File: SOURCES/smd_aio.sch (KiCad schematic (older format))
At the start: 44 parts, among them P2 CONN_01X03, P3 CONN_02X05, P4 STDCONN, Q1 BSS123, Q2 BSS123, Q3 BSS123, Q4 BSS123, Q5 FZT751TA, SW1 SW_PUSH, U2 24AA256SN

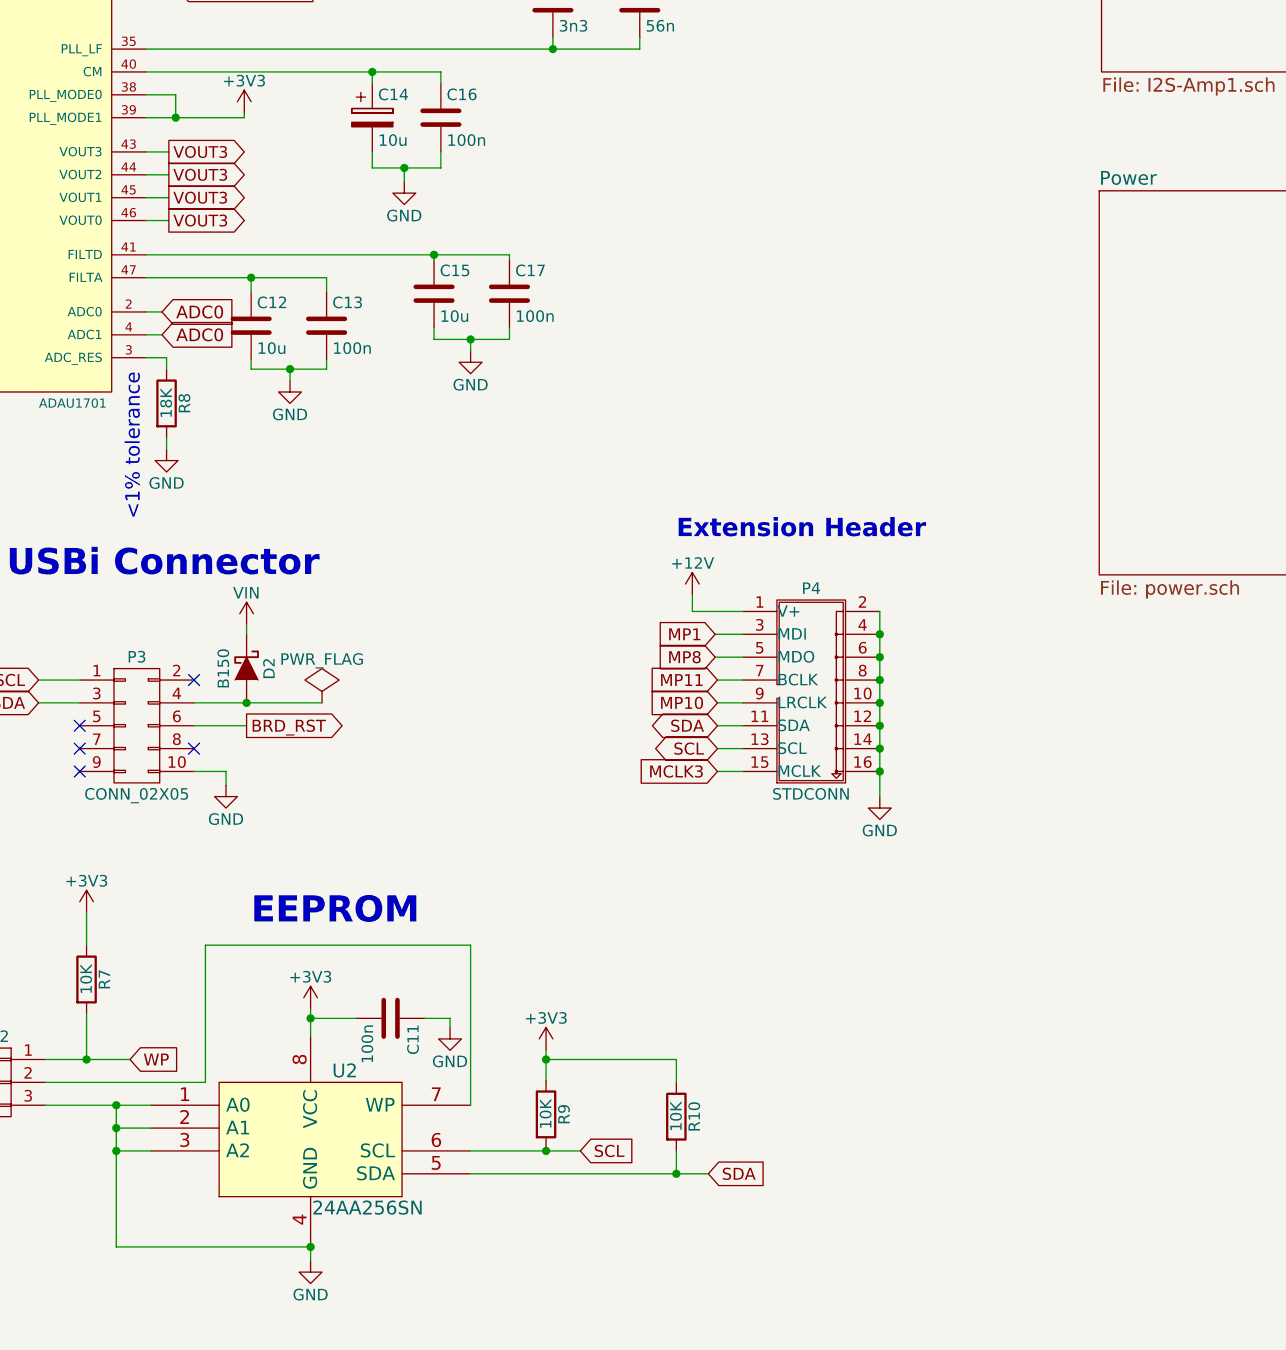
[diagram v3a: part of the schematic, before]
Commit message: added SPDIF lib & analog out
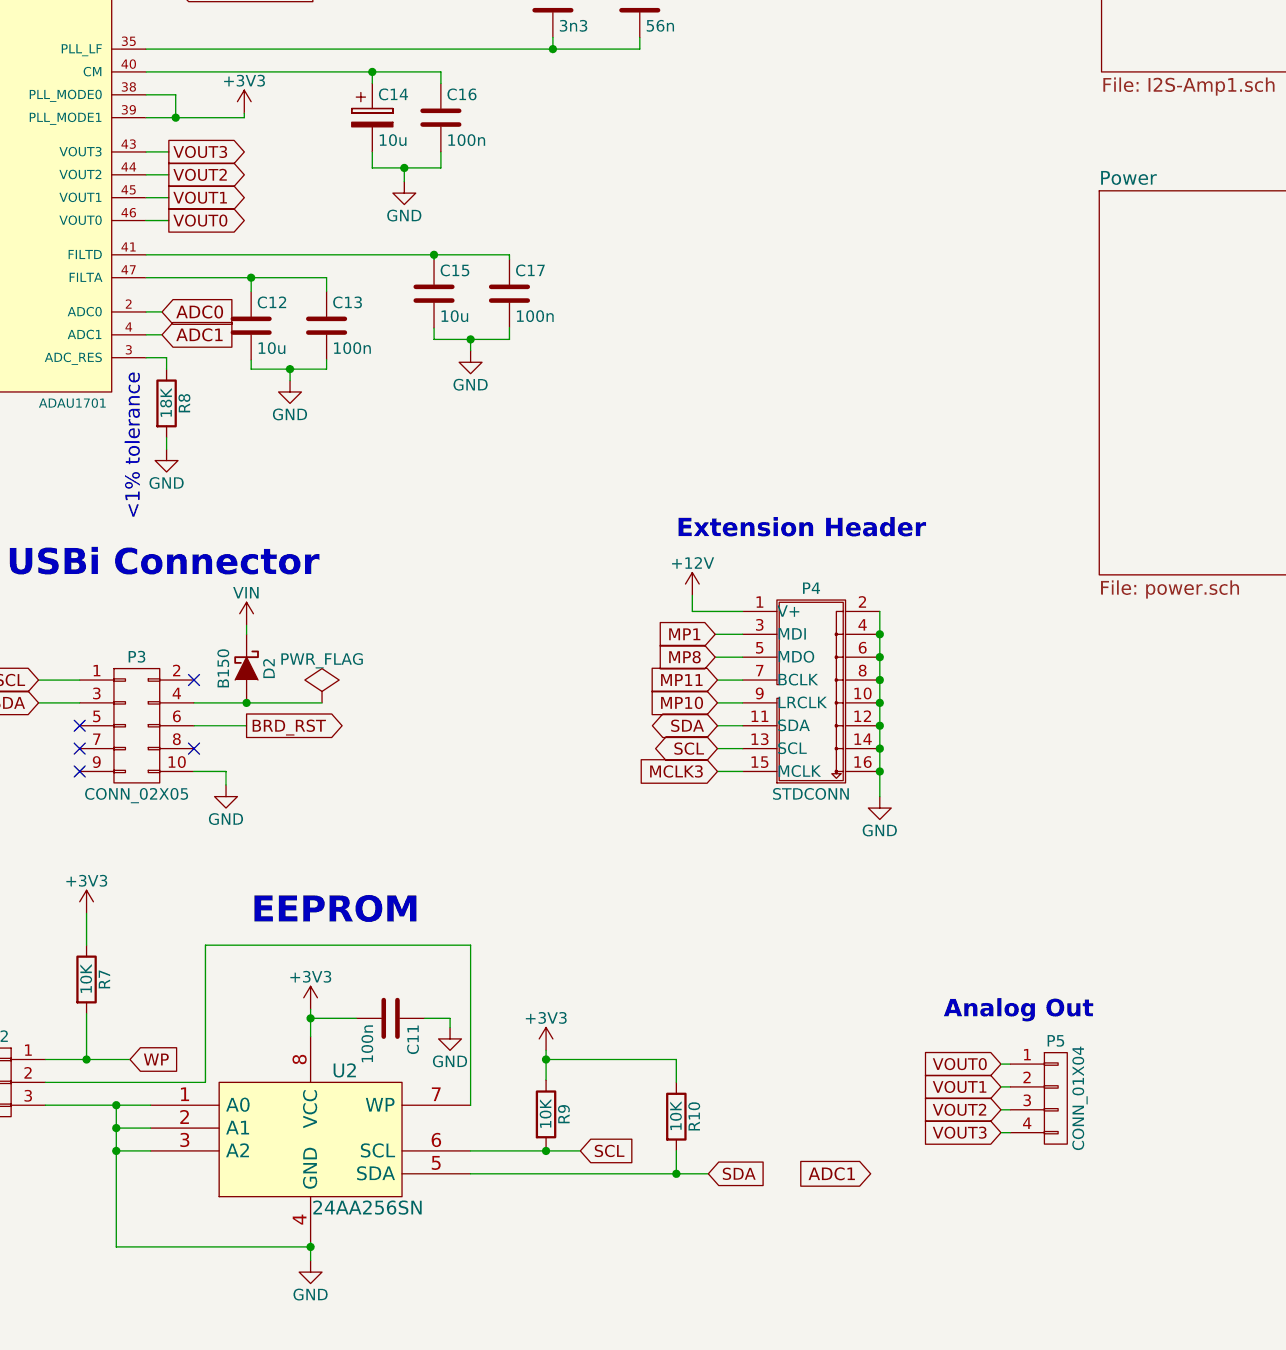
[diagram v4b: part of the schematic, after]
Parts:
- added P5: CONN_01X04, fdsp_pinheader:Pin_Header_Angled_1x04, symbol CONN_01X04
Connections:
- net ADC0: no longer U?.4 (ADC1)
- net VOUT3: now also P5.4 (P4); no longer U?.44 (VOUT2), U?.45 (VOUT1), U?.46 (VOUT0)
- new net ADC1: U?.4 (ADC1)
- new net VOUT0: P5.1 (P1), U?.46 (VOUT0)
- new net VOUT1: P5.2 (P2), U?.45 (VOUT1)
- new net VOUT2: P5.3 (P3), U?.44 (VOUT2)
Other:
- note added: "Analog Out"
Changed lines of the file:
@@
 LIBS:Polarized_Cap
 LIBS:tas5760mdcar
+LIBS:symbols-CS8422-CNZ
+LIBS:symbols_CS8406-CZZ
 LIBS:smd_aio-cache
 EELAYER 25 0
@@
 VOUT3
 Text GLabel 5300 3370 2    51   Output ~ 0
-VOUT3
+VOUT2
 Text GLabel 5300 3470 2    51   Output ~ 0
-VOUT3
+VOUT1
 Text GLabel 5300 3570 2    51   Output ~ 0
-VOUT3
+VOUT0
 $Comp
 L C C12
@@
 ADC0
 Text GLabel 5270 4070 2    55   Input ~ 0
-ADC0
+ADC1
 $Comp
 L R R8
@@
 Text Notes 7520 4970 0    80   ~ 16
 Extension Header
+Text Notes 8690 7070 0    76   ~ 15
+Analog Out
+Text GLabel 8940 7260 0    51   Input ~ 0
+VOUT0
+Text GLabel 8940 7460 0    51   Input ~ 0
+VOUT2
+Text GLabel 8940 7360 0    51   Input ~ 0
+VOUT1
+Text GLabel 8940 7560 0    51   Input ~ 0
+VOUT3
+Text GLabel 8370 7740 0    55   Input ~ 0
+ADC1
+$Comp
+L CONN_01X04 P5
+U 1 1 5B050B23
+P 9180 7410
+F 0 "P5" H 9180 7660 50  0000 C CNN
+F 1 "CONN_01X04" V 9280 7410 50  0000 C CNN
+F 2 "fdsp_pinheader:Pin_Header_Angled_1x04" H 9180 7410 60  0001 C CNN
+F 3 "" H 9180 7410 60  0000 C CNN
+	1    9180 7410
+	1    0    0    -1
+$EndComp
+Wire Wire Line
+	8940 7260 8980 7260
+Wire Wire Line
+	8940 7360 8980 7360
+Wire Wire Line
+	8940 7460 8980 7460
+Wire Wire Line
+	8940 7560 8980 7560
 $EndSCHEMATC

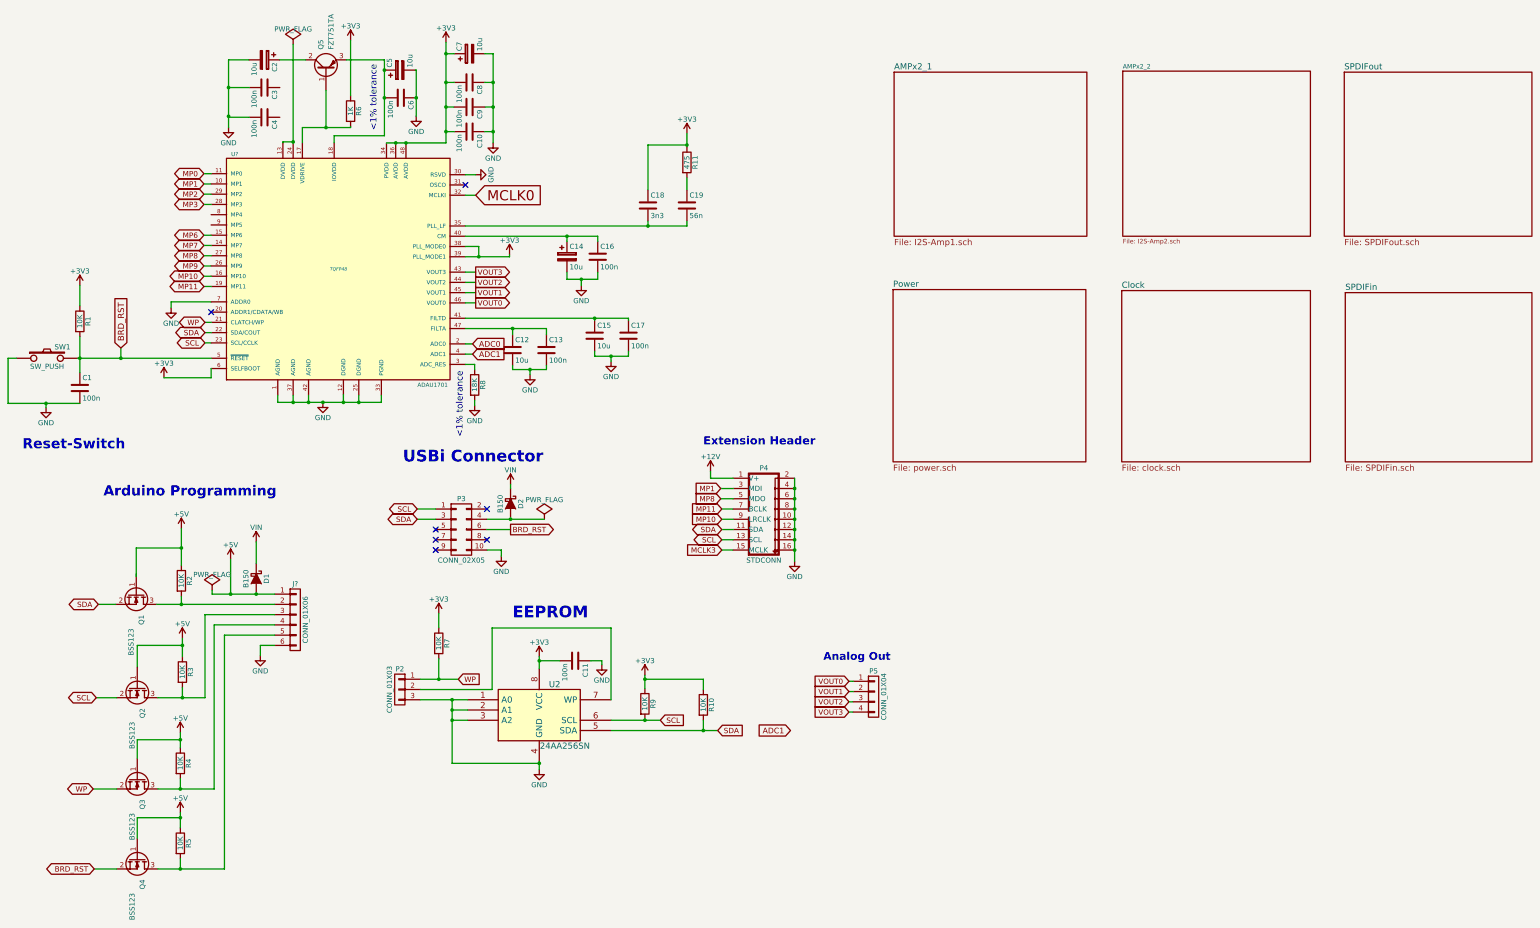
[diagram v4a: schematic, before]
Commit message: added analog input
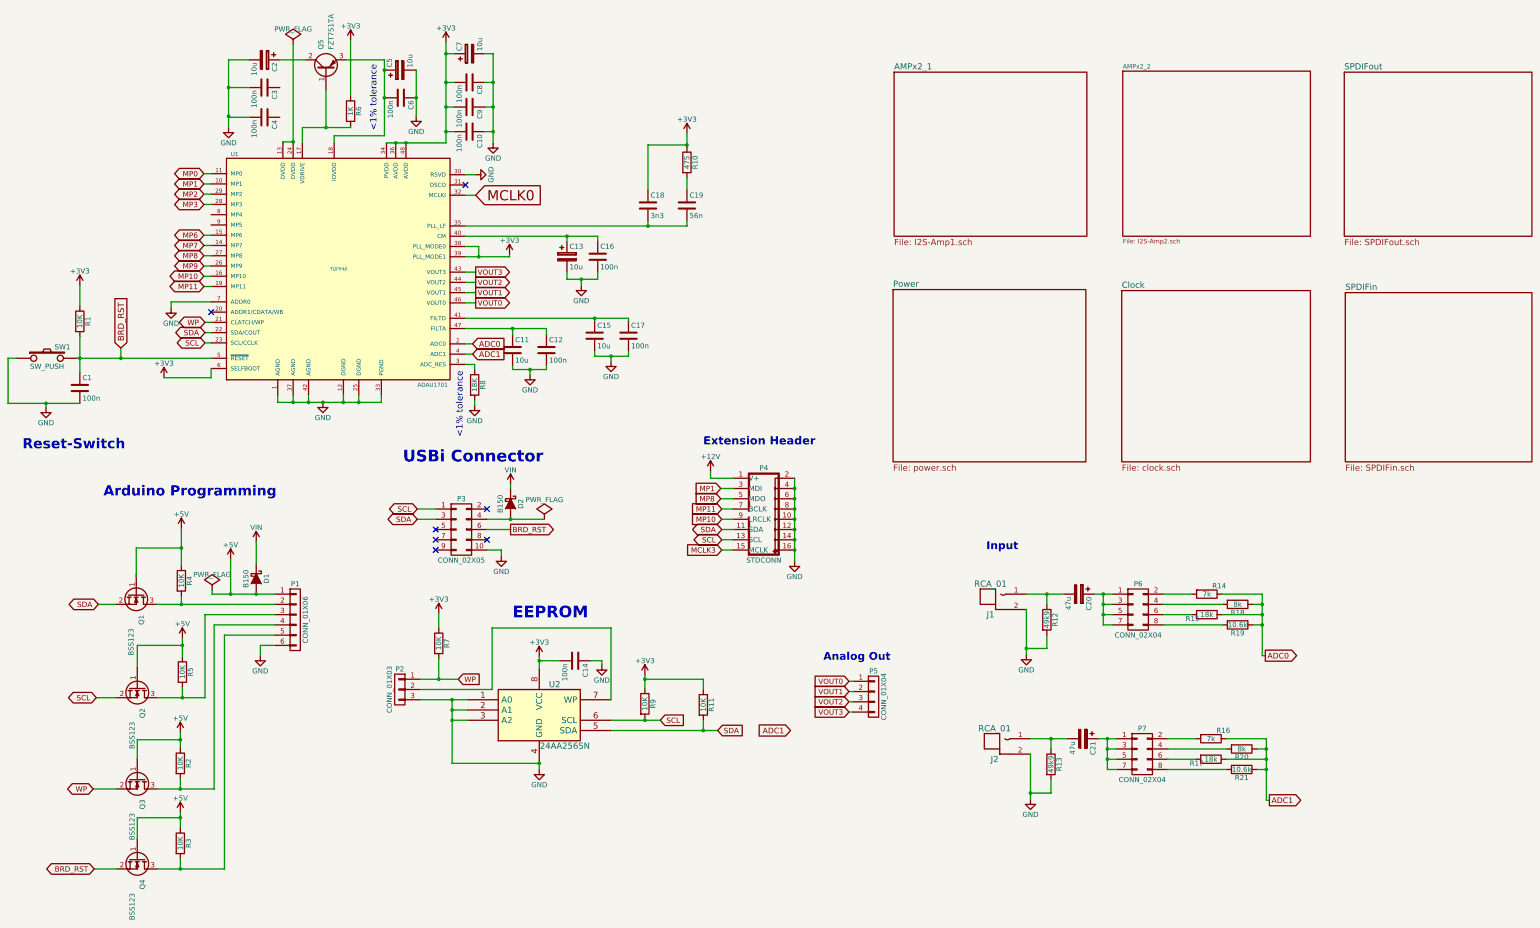
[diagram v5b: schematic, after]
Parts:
- added C20, C21: 47u, fdsp_capacitor:C_Radial_D5_L11_P2, symbol CP
- added J1, J2: RCA_01, fdsp_connector:RCA_RCJ-01x, symbol RCA_01
- added P6, P7: CONN_02X04, fdsp_pinheader:Pin_Header_Straight_2x04, symbol CONN_02X04
- added R12, R13: 49k9, fdsp_resistor:R_1206_HandSoldering, symbol R
- added R14, R16: 7k, fdsp_resistor:R_1206_HandSoldering, symbol R
- added R15, R17: 18k, fdsp_resistor:R_1206_HandSoldering, symbol R
- added R18, R20: 8k, fdsp_resistor:R_1206_HandSoldering, symbol R
- added R19, R21: 10.6k, fdsp_resistor:R_1206_HandSoldering, symbol R
- P1: renamed from J?; footprint (none) -> fdsp_pinheader:Pin_Header_Straight_1x06
- gave numbers to parts that had none: 1
- renumbered C12 to C11, C13 to C12, C14 to C13, C11 to C14, R11 to R10, R10 to R11, R4 to R2, R5 to R3, R2 to R4, R3 to R5
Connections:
- net ADC0: now also R14.1, R15.1, R18.1, R19.1
- net ADC1: now also R16.1, R17.1, R20.1, R21.1
- net GND: now also J1.2 (GND), J2.2 (GND), R12.2, R13.2
- new net: C20.2, J1.1 (SIG), R12.1
- new net: C20.1, P6.1 (P1), P6.3 (P3), P6.5 (P5), P6.7 (P7)
- new net: P6.2 (P2), R14.2
- new net: P6.4 (P4), R18.2
- new net: P6.6 (P6), R15.2
- new net: P6.8 (P8), R19.2
- new net: C21.2, J2.1 (SIG), R13.1
- new net: C21.1, P7.1 (P1), P7.3 (P3), P7.5 (P5), P7.7 (P7)
- new net: P7.2 (P2), R16.2
- new net: P7.4 (P4), R20.2
- new net: P7.6 (P6), R17.2
- new net: P7.8 (P8), R21.2
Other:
- note added: "Input"

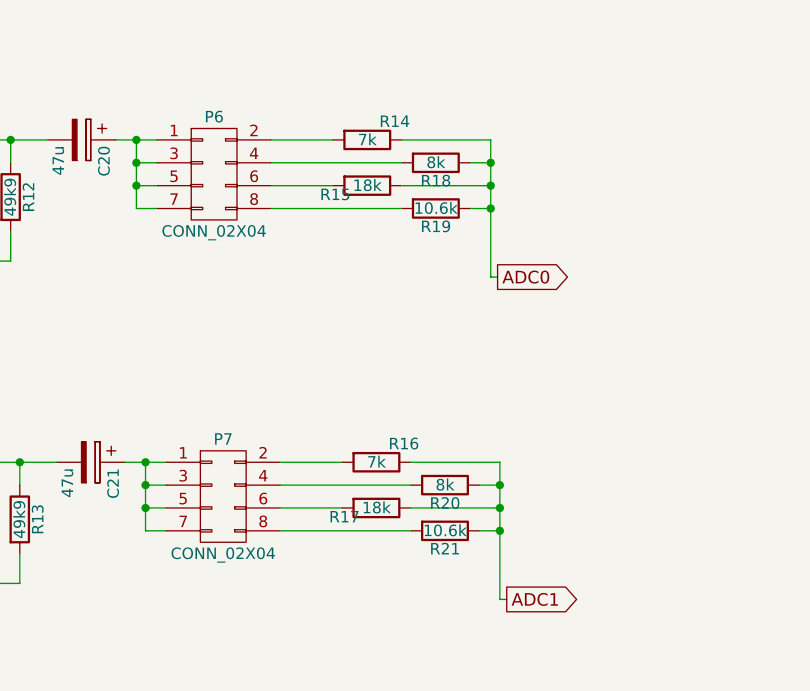
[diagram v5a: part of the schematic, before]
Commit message: added clock + extended lib
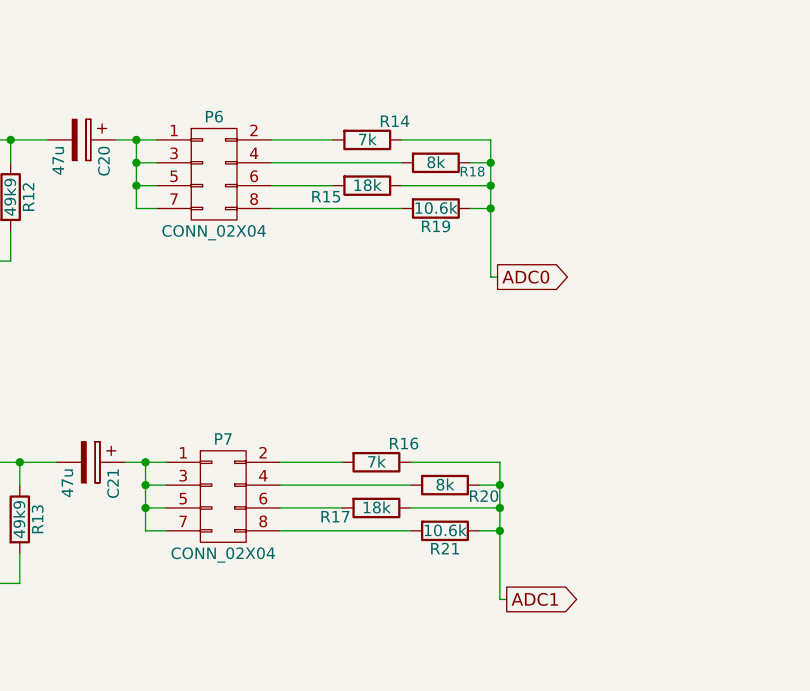
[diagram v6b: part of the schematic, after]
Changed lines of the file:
@@
 LIBS:symbols-CS8422-CNZ
 LIBS:symbols_CS8406-CZZ
+LIBS:smd_aio-lib
+LIBS:fdsp_device_new
+LIBS:fdsp_digital_new
+LIBS:fdsp_linear_new
+LIBS:fdsp_oscillator_new
+LIBS:fdsp_transistor_new
 LIBS:smd_aio-cache
 EELAYER 25 0
@@
 U 1 1 5B0660AB
 P 12730 6510
-F 0 "R18" V 12810 6510 50  0000 C CNN
+F 0 "R18" V 12770 6670 42  0000 C CNN
 F 1 "8k" V 12730 6510 50  0000 C CNN
 F 2 "fdsp_resistor:R_1206_HandSoldering" H 12660 6510 30  0001 C CNN
@@
 U 1 1 5B0661A6
 P 12430 6610
-F 0 "R15" V 12470 6470 50  0000 C CNN
+F 0 "R15" V 12480 6430 50  0000 C CNN
 F 1 "18k" V 12430 6610 50  0000 C CNN
 F 2 "fdsp_resistor:R_1206_HandSoldering" V 12360 6610 30  0001 C CNN
@@
 U 1 1 5B06B331
 P 12770 7920
-F 0 "R20" V 12850 7920 50  0000 C CNN
+F 0 "R20" V 12820 8090 50  0000 C CNN
 F 1 "8k" V 12770 7920 50  0000 C CNN
 F 2 "fdsp_resistor:R_1206_HandSoldering" H 12700 7920 30  0001 C CNN
@@
 U 1 1 5B06B337
 P 12470 8020
-F 0 "R17" V 12510 7880 50  0000 C CNN
+F 0 "R17" V 12510 7840 50  0000 C CNN
 F 1 "18k" V 12470 8020 50  0000 C CNN
 F 2 "fdsp_resistor:R_1206_HandSoldering" V 12400 8020 30  0001 C CNN

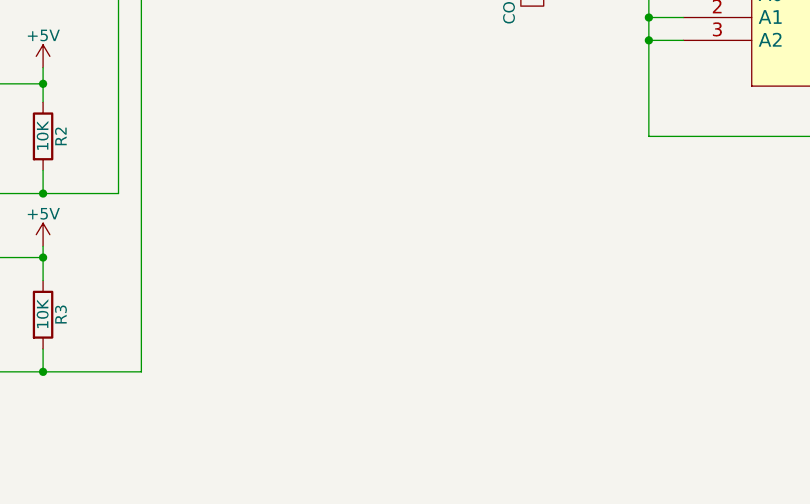
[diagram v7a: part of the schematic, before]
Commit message: IDT2309 clock buffer added
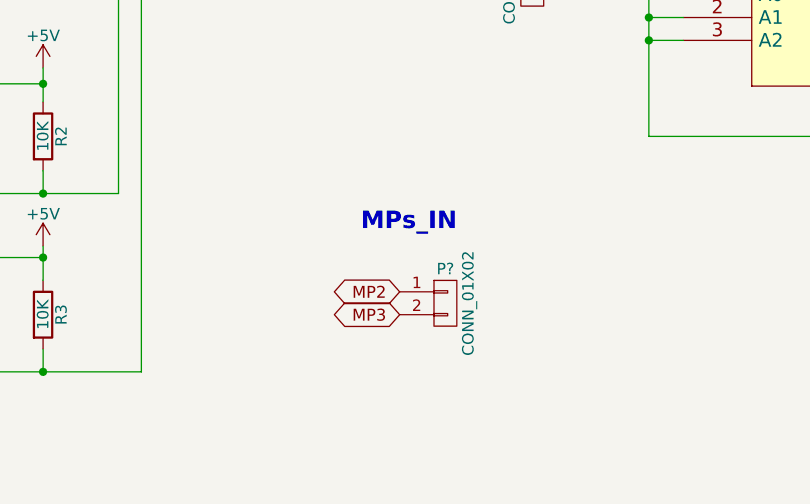
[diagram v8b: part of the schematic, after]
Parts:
- added P?: CONN_01X02, symbol CONN_01X02
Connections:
- net MP2: now also P?.1 (P1)
- net MP3: now also P?.2 (P2)
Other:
- note added: "MPs_IN"
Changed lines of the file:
@@
 Text Notes 10280 5990 0    76   ~ 15
 Input
+$Comp
+L CONN_01X02 P?
+U 1 1 5B102BB9
+P 4180 8790
+F 0 "P?" H 4180 8940 50  0000 C CNN
+F 1 "CONN_01X02" V 4280 8790 50  0000 C CNN
+F 2 "" H 4180 8790 60  0000 C CNN
+F 3 "" H 4180 8790 60  0000 C CNN
+	1    4180 8790
+	1    0    0    -1
+$EndComp
+Text GLabel 3980 8740 0    52   BiDi ~ 0
+MP2
+Text GLabel 3980 8840 0    52   BiDi ~ 0
+MP3
+Text Notes 3810 8480 0    76   ~ 15
+MPs_IN
 $EndSCHEMATC
